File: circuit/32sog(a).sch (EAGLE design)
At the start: 16 parts, among them IC1 MEGA8-P, K1 PG203J, X1 16.0

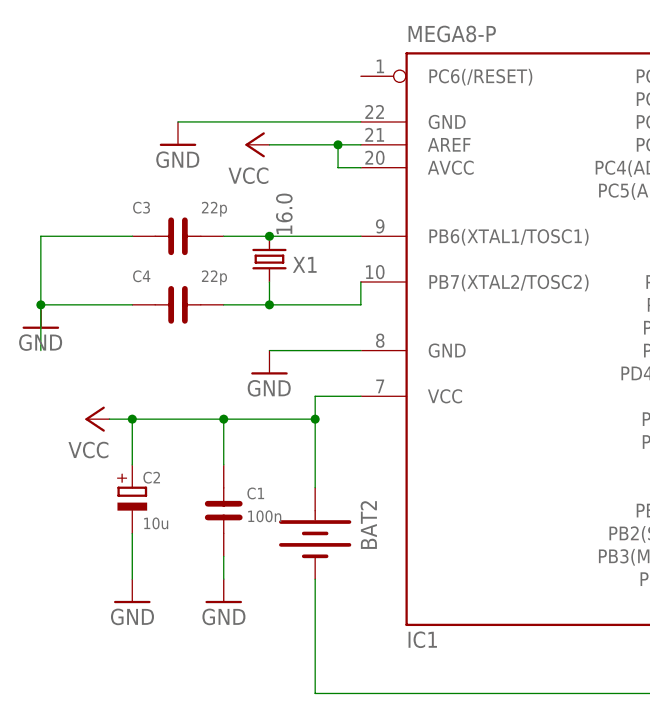
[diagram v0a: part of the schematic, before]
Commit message: Added pull-up resistor on RESET line
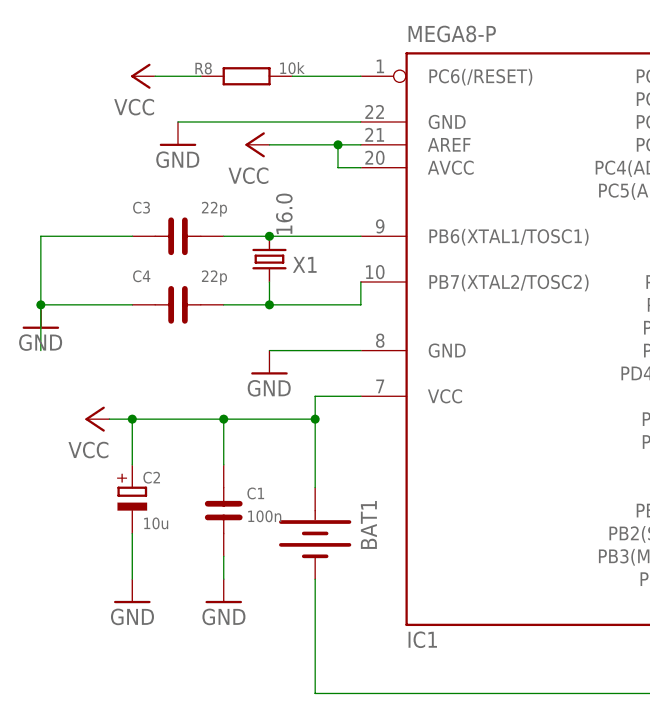
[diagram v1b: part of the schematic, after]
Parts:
- added R8: 10k, rcl:R-EU_0207/7
- renumbered BAT2 to BAT1
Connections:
- new net N$3: IC1.PC6(/RESET), R8.2
- net VCC: now also R8.1
